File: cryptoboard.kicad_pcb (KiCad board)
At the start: 2 copper layers, 53.3 x 50.8 mm, 32 parts, among them J1 USB_A, J2 BOOT, J3 SWD, J4 USR_LEFT, J5 USR_RIGHT, J6 Conn_01x04, SW1 SW_Push, U1 STM32F103C8Tx, U2 LM317_SOT-223-3.3V

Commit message: add wiring
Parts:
- moved J1 43.5 mm to (76.1, 32.3), turned to 90 degrees
- moved JP1 43.0 mm to (33.0, 72.0), turned to 90 degrees
- moved C1 39.9 mm to (71.9, 33.5), turned to 90 degrees
- moved J2 37.4 mm to (27.9, 45.7)
- moved J3 35.6 mm to (27.9, 61.0)
- moved C3 32.5 mm to (59.3, 32.3), turned to 90 degrees
- moved C2 32.2 mm to (61.0, 32.2), turned to -90 degrees
- moved J4 26.2 mm to (76.2, 45.7), turned to -90 degrees
- moved J5 24.0 mm to (63.5, 55.9), turned to 90 degrees
- moved C5 23.5 mm to (56.3, 48.8)
- moved U2 21.2 mm to (66.0, 31.1), turned to 90 degrees
- moved R7 21.0 mm to (32.3, 66.9), turned to 90 degrees
- moved C4 20.5 mm to (55.4, 58.8), turned to -90 degrees
- moved SW1 20.4 mm to (31.0, 55.7)
- moved R8 20.2 mm to (38.8, 71.1), turned to -90 degrees
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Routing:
- net +3.3V: track 0.00 -> 78.1 mm
- net SWCLK: track 0.00 -> 32.0 mm
- net +5V: track 0.00 -> 29.5 mm
- net LED1: track 0.00 -> 23.2 mm, vias 0 -> 2
- net LED2: track 0.00 -> 22.5 mm, vias 0 -> 2
- net RESET: track 0.00 -> 18.7 mm
- net PA12: track 0.00 -> 16.4 mm
- net PA11: track 0.00 -> 16.3 mm
- net SDA: track 0.00 -> 7.81 mm
- net SWDIO: track 0.00 -> 7.26 mm
- net Net-(J3-Pin_5): track 0.00 -> 5.43 mm
- net SCL: track 0.00 -> 4.95 mm
- net Net-(KEYBOARD1-D-): track 0.00 -> 4.59 mm
- net Net-(KEYBOARD1-D+): track 0.00 -> 4.59 mm

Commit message: add wiring
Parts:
- J2: footprint Connector_PinHeader_2.54mm:PinHeader_2x03_P2.54mm_Vertical -> Library:PinHeader_2x03_P2.54mm_Vertical_new
- moved J4 5.08 mm to (76.2, 40.6)
- moved J5 5.08 mm to (63.5, 61.0)
- moved C8 2.77 mm to (36.4, 60.0)
- turned R1 to 180 degrees
- turned R2 to 180 degrees
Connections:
- U1 pad 18: unconnected-(U1-PB0-Pad18) -> INT
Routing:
- net +5V: track 29.5 -> 131.3 mm
- net +3.3V: track 78.1 -> 167.8 mm, vias 0 -> 4
- net SWDIO: track 7.26 -> 40.3 mm, vias 0 -> 2
- net BOOT1: track 0.00 -> 29.3 mm, vias 0 -> 2
- net MOSI: track 0.00 -> 24.3 mm
- net ETH_RST: track 0.00 -> 24.2 mm, vias 0 -> 2
- net SCLK: track 0.00 -> 23.5 mm, vias 0 -> 2
- net SCL: track 4.95 -> 25.3 mm, vias 0 -> 2
- net SDA: track 7.81 -> 27.5 mm, vias 0 -> 2
- net INT: track 0.00 -> 18.2 mm
- net BOOT0: track 0.00 -> 15.2 mm, vias 0 -> 2
- net RESET: track 18.7 -> 31.4 mm, vias 0 -> 2
- net MISO: track 0.00 -> 11.2 mm
- net Net-(J2-Pin_2): track 0.00 -> 6.12 mm
- net Net-(J2-Pin_5): track 0.00 -> 5.24 mm
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
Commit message: add wiring
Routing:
- net GND: track 0.00 -> 11.3 mm, vias 0 -> 21
- net SWCLK: track 32.5 -> 34.1 mm
- net SWDIO: track 40.3 -> 41.7 mm
- added copper zone on B.Cu, net GND
- added copper zone on F.Cu, net GND

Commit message: fill ground
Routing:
- net GND: vias 21 -> 26
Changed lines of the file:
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@@
   (segment (start 51.55 57.5025) (end 51.55 59.45) (width 0.25) (layer "F.Cu") (net 2))
   (via (at 40 63.5) (size 0.8) (drill 0.4) (layers "F.Cu" "B.Cu") (free) (net 2))
+  (via (at 28 36) (size 0.8) (drill 0.4) (layers "F.Cu" "B.Cu") (free) (net 2))
+  (via (at 42 48) (size 0.8) (drill 0.4) (layers "F.Cu" "B.Cu") (free) (net 2))
   (via (at 77.5 44.5) (size 0.8) (drill 0.4) (layers "F.Cu" "B.Cu") (free) (net 2))
   (via (at 71.5 72) (size 0.8) (drill 0.4) (layers "F.Cu" "B.Cu") (free) (net 2))
@@
   (via (at 71.5 30) (size 0.8) (drill 0.4) (layers "F.Cu" "B.Cu") (free) (net 2))
   (via (at 69 36.5) (size 0.8) (drill 0.4) (layers "F.Cu" "B.Cu") (free) (net 2))
+  (via (at 37 49.5) (size 0.8) (drill 0.4) (layers "F.Cu" "B.Cu") (free) (net 2))
   (via (at 61.5 67) (size 0.8) (drill 0.4) (layers "F.Cu" "B.Cu") (free) (net 2))
   (via (at 43 55.5) (size 0.8) (drill 0.4) (layers "F.Cu" "B.Cu") (free) (net 2))
@@
   (via (at 37 70) (size 0.8) (drill 0.4) (layers "F.Cu" "B.Cu") (free) (net 2))
   (via (at 28 42) (size 0.8) (drill 0.4) (layers "F.Cu" "B.Cu") (free) (net 2))
+  (via (at 35.5 34.5) (size 0.8) (drill 0.4) (layers "F.Cu" "B.Cu") (free) (net 2))
   (via (at 33.5 64) (size 0.8) (drill 0.4) (layers "F.Cu" "B.Cu") (free) (net 2))
+  (via (at 38.5 54) (size 0.8) (drill 0.4) (layers "F.Cu" "B.Cu") (free) (net 2))
   (via (at 35.5 28) (size 0.8) (drill 0.4) (layers "F.Cu" "B.Cu") (free) (net 2))
   (via (at 67 56) (size 0.8) (drill 0.4) (layers "F.Cu" "B.Cu") (free) (net 2))

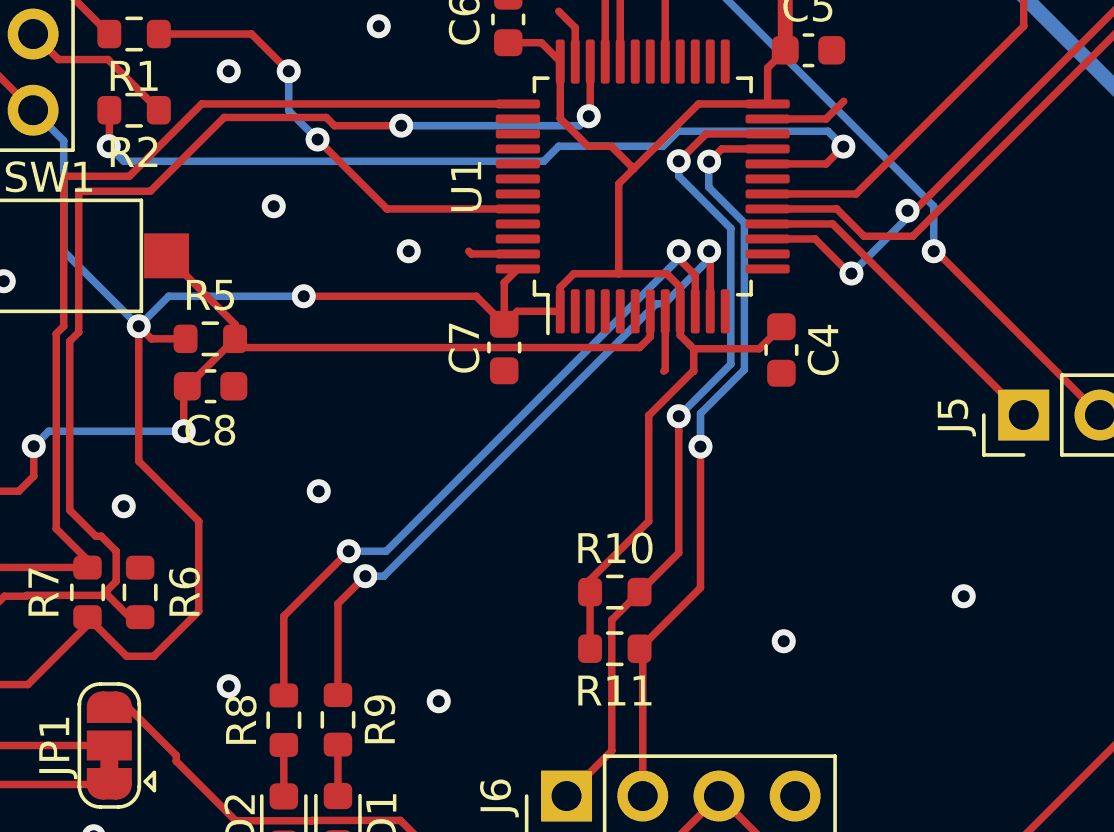
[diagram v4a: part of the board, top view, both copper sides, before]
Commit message: add crystal psb
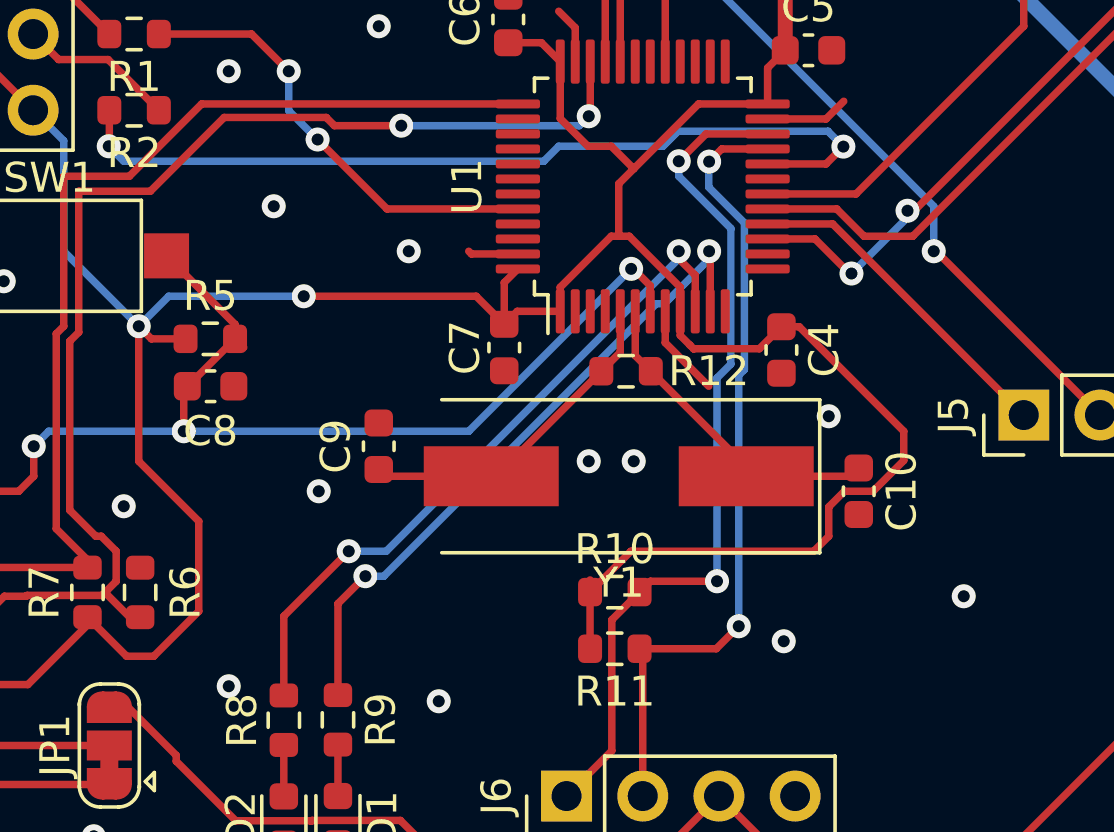
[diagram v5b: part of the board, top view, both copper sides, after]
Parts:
- added C10: 20p, Capacitor_SMD:C_0603_1608Metric, F.Cu at (58.0, 63.5)
- added C9: 20p, Capacitor_SMD:C_0603_1608Metric, F.Cu at (42.0, 62.0)
- added R12: 1M, Resistor_SMD:R_0603_1608Metric, F.Cu at (50.2, 59.5)
- added Y1: Crystal, Crystal:Crystal_SMD_HC49-SD, F.Cu at (50.0, 63.0)
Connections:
- U1 pad 5: unconnected-(U1-PD0-Pad5) -> OSIN
- U1 pad 6: unconnected-(U1-PD1-Pad6) -> OSOUT
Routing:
- net OSIN: track 0.00 -> 11.2 mm
- net OSOUT: track 0.00 -> 10.9 mm
- net +3.3V: track 167.7 -> 177.7 mm
- net RESET: track 31.4 -> 35.8 mm, vias 2 -> 3
- net SCL: track 25.3 -> 26.8 mm
- net SDA: track 27.5 -> 28.8 mm
- net GND: track 11.3 -> 12.3 mm, vias 26 -> 29
